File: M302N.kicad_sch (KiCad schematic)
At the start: 35 parts, among them J1 DC12V, J10 ADC_IN, J11 RJ45, J12 DC12V FAN, J13 Conn_01x05_Socket, J14 Conn_01x05_Socket, J15 Conn_01x05_Pin, J16 Conn_01x05_Pin, J17 Conn_01x08_Pin, J18 Conn_01x04_Socket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

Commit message: V2.00はじめ
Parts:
- removed J10, J9: ADC_IN, Connector_JST:JST_XH_B3B-XH-A_1x03_P2.50mm_Vertical, symbol Connector_Generic:Conn_01x03
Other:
- title: M302N -> M302N (under constructions)

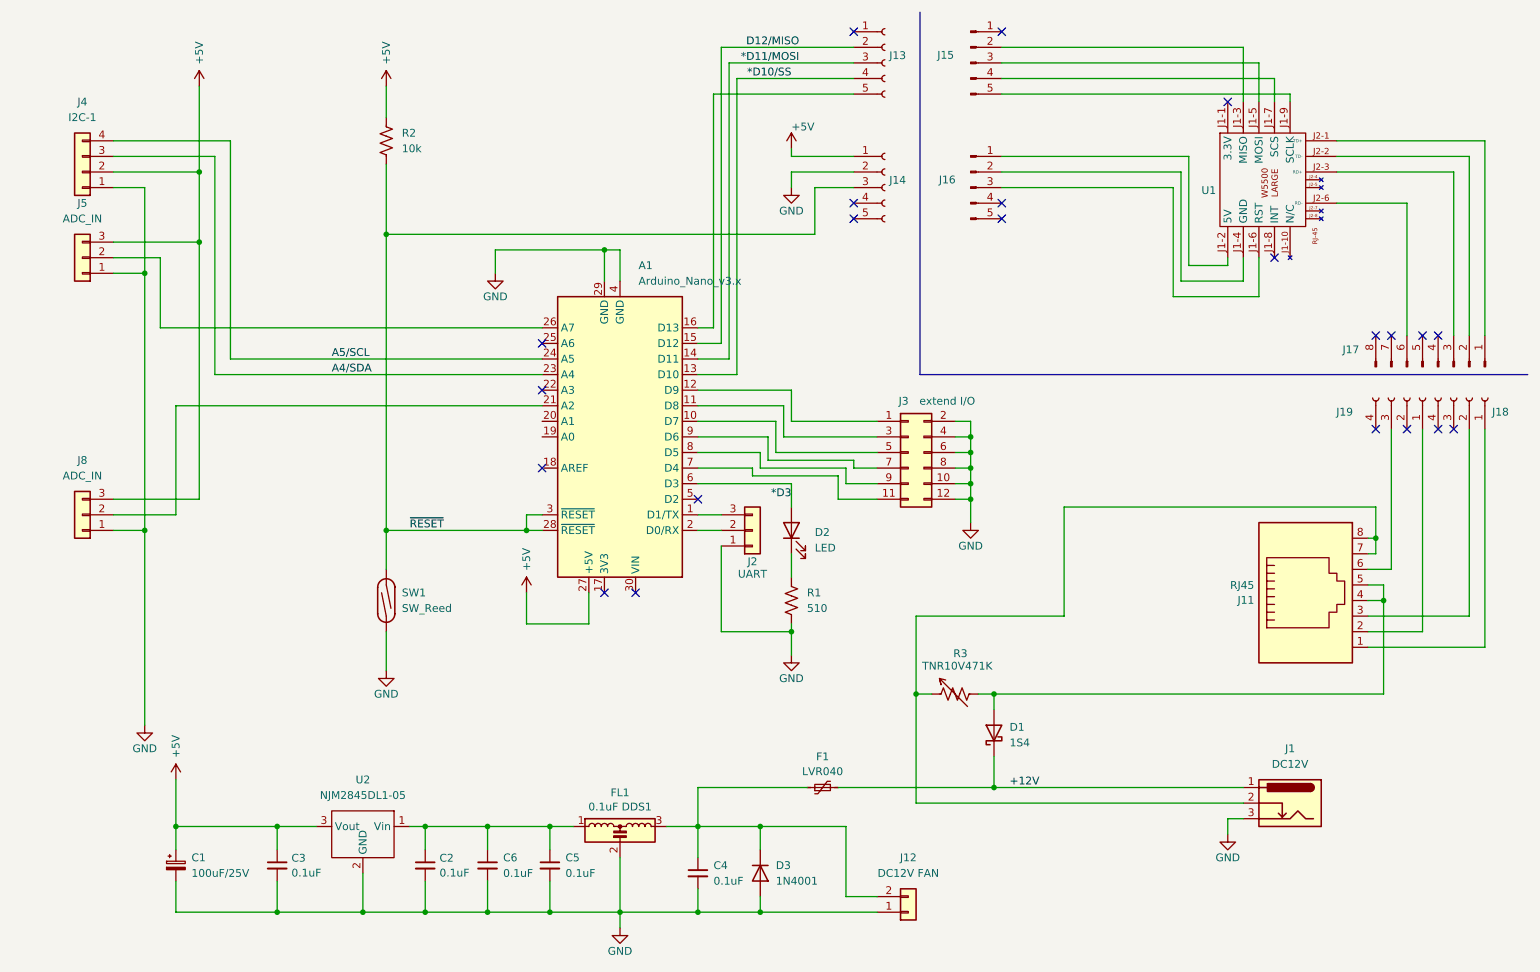
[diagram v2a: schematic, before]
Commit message: 回路図上の変更は完了。PCB部品の選定に入る所。
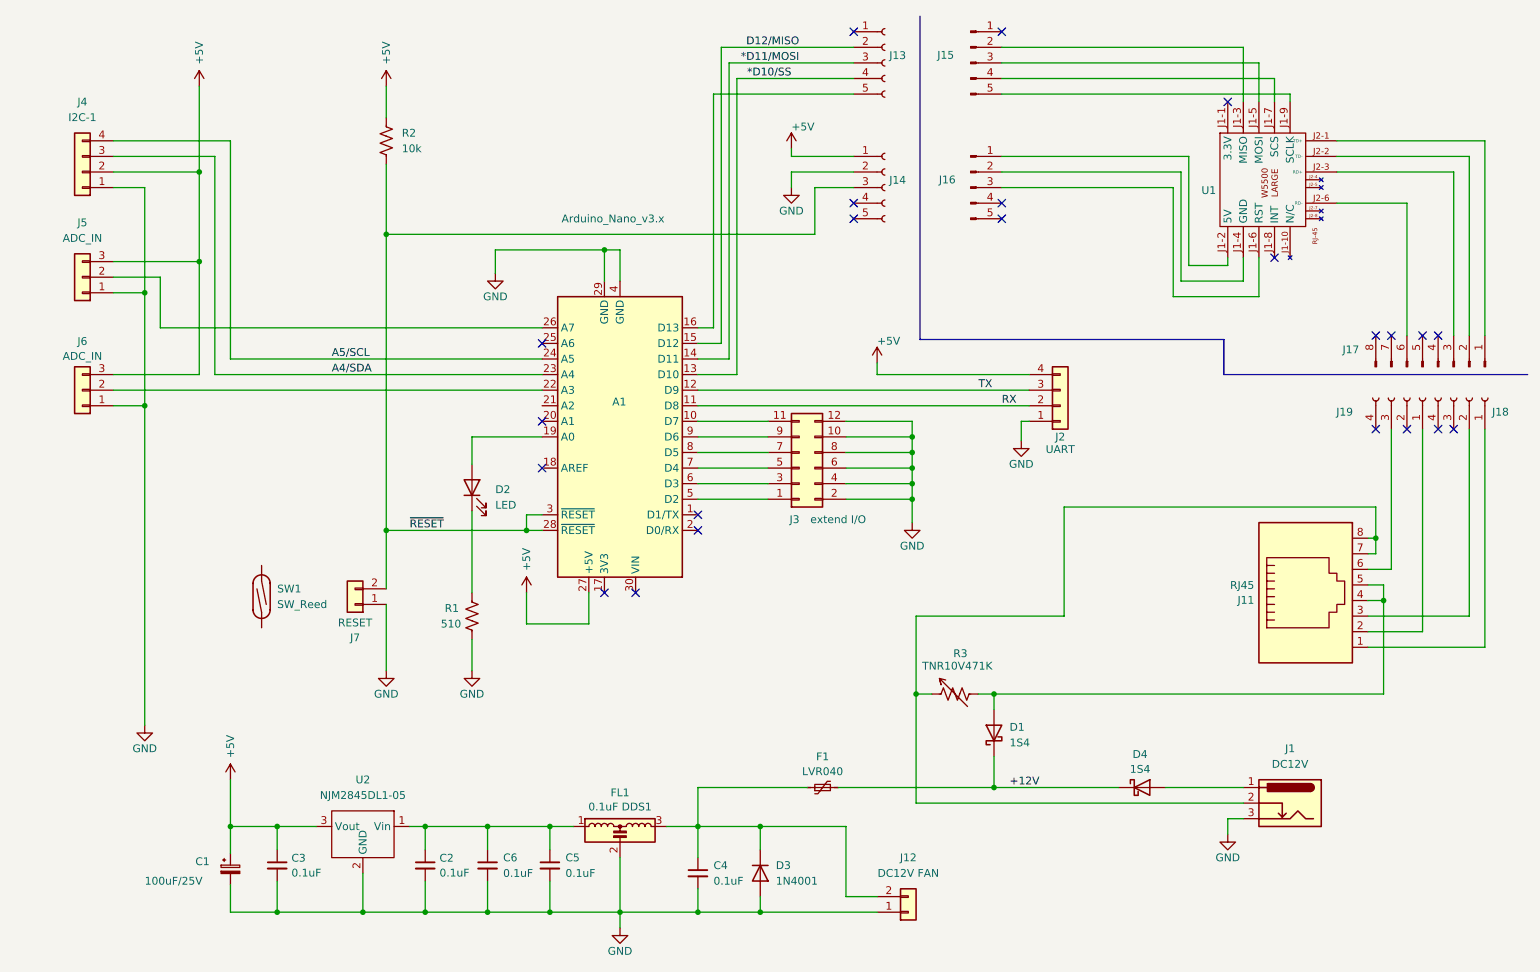
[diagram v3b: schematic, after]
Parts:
- added D4: 1S4, Resistor_THT:R_Axial_DIN0204_L3.6mm_D1.6mm_P5.08mm_Horizontal, symbol Device:D_Schottky
- added J7: RESET, Connector_JST:JST_XH_S2B-XH-A_1x02_P2.50mm_Horizontal, symbol Connector_Generic:Conn_01x02
- J2: footprint Connector_PinHeader_2.54mm:PinHeader_1x03_P2.54mm_Vertical -> Connector_PinHeader_2.54mm:PinHeader_1x04_P2.54mm_Vertical; symbol Connector_Generic:Conn_01x03 -> Connector_Generic:Conn_01x04
- J5: footprint Connector_JST:JST_XH_S3B-XH-A_1x03_P2.50mm_Horizontal -> Connector_JST:JST_XH_B3B-XH-A_1x03_P2.50mm_Vertical
- SW1: now left out of the parts list
- renumbered J8 to J6
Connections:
- net +12V: now also D4.1 (K); no longer J1.1
- net +5V: now also J2.4 (Pin_4)
- net GND: now also J7.1 (Pin_1); no longer SW1.1
- net ~{RESET}: now also J7.2 (Pin_2); no longer SW1.2
- net at A1.2 (D0/RX): no longer J2.2 (Pin_2)
- net at A1.1 (D1/TX): no longer J2.3 (Pin_3)
- net at J3.1 (Pin_1): now also A1.5 (D2); no longer A1.12 (D9)
- net at J3.11 (Pin_11): now also A1.10 (D7); no longer A1.7 (D4)
- net at J3.3 (Pin_3): now also A1.6 (D3); no longer A1.11 (D8)
- net at J3.5 (Pin_5): now also A1.7 (D4); no longer A1.10 (D7)
- net at J3.7 (Pin_7): now also A1.8 (D5); no longer A1.9 (D6)
- net at J3.9 (Pin_9): now also A1.9 (D6); no longer A1.8 (D5)
- net at J6.2 (Pin_2): now also A1.22 (A3); no longer A1.21 (A2)
- net at A1.19 (A0): now also D2.2 (A)
- removed net *D3: A1.6 (D3), D2.2 (A)
- new net: D4.2 (A), J1.1
- new net RX: A1.11 (D8), J2.2 (Pin_2)
- new net TX: A1.12 (D9), J2.3 (Pin_3)
- no-connect marks 22 -> 23
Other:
- moved on the sheet: C1, D2, J3, J5, J6, R1, SW1

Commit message: v2.00 PCB変更とスイッチングレギュレータ採用検討
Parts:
- J2: footprint Connector_PinHeader_2.54mm:PinHeader_1x04_P2.54mm_Vertical -> Connector_JST:JST_XH_S4B-XH-A_1x04_P2.50mm_Horizontal
- J5: footprint Connector_JST:JST_XH_B3B-XH-A_1x03_P2.50mm_Vertical -> Connector_JST:JST_XH_S3B-XH-A_1x03_P2.50mm_Horizontal
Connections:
- no-connect marks 23 -> 24
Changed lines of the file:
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@@
 	)
 	(no_connect
+		(at 123.19 78.74)
+	)
+	(no_connect
 		(at 234.95 29.21)
 	)
@@
 			)
 		)
-		(property "Footprint" "Connector_JST:JST_XH_B3B-XH-A_1x03_P2.50mm_Vertical"
+		(property "Footprint" "Connector_JST:JST_XH_S3B-XH-A_1x03_P2.50mm_Horizontal"
 			(at 48.26 57.785 0)
 			(effects
@@
 			)
 		)
-		(property "Footprint" "Connector_PinHeader_2.54mm:PinHeader_1x04_P2.54mm_Vertical"
+		(property "Footprint" "Connector_JST:JST_XH_S4B-XH-A_1x04_P2.50mm_Horizontal"
 			(at 207.645 78.74 0)
 			(effects

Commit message: DCDC converter
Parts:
- removed C3: 0.1uF, Capacitor_THT:C_Disc_D4.3mm_W1.9mm_P5.00mm, symbol Device:C_Small
- removed U2: NJM2845DL1-05, Package_TO_SOT_SMD:TO-252-3_TabPin2, symbol holly:NJM2845DL1
- added U2: BP5293-50, SIP03_BP5293_17X7P2_ROM, symbol 2025-06-02_10-47-13:BP5293-50
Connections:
- net +5V: now also U2.3 (VOUT)
- net GND: now also U2.2 (GND)
- net at C2.1, C5.1, C6.1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: now also U2.1 (VIN)
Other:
- moved on the sheet: C1

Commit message: 大胆な変更
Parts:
- removed C6: 0.1uF, Capacitor_THT:C_Disc_D4.3mm_W1.9mm_P5.00mm, symbol Device:C_Small
- U2: footprint SIP03_BP5293_17X7P2_ROM -> footprints:SIP03_BP5293_17X7P2_ROM; symbol 2025-06-02_10-47-13:BP5293-50 -> M302N-symlib:BP5293-50
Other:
- moved on the sheet: C2, U2
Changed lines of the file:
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@@
 	)
 	(junction
-		(at 104.14 161.29)
-		(diameter 0)
-		(color 0 0 0 0)
-	)
-	(junction
 		(at 133.35 53.34)
 		(diameter 0)
@@
 	)
 	(junction
-		(at 148.59 161.29)
+		(at 111.76 161.29)
 		(diameter 0)
 		(color 0 0 0 0)
 	)
 	(junction
-		(at 97.79 50.8)
+		(at 111.76 147.32)
 		(diameter 0)
 		(color 0 0 0 0)
 	)
 	(junction
-		(at 183.515 83.82)
+		(at 148.59 161.29)
 		(diameter 0)
 		(color 0 0 0 0)
 	)
 	(junction
-		(at 183.515 93.98)
+		(at 97.79 50.8)
 		(diameter 0)
 		(color 0 0 0 0)
 	)
 	(junction
-		(at 114.3 147.32)
+		(at 183.515 83.82)
 		(diameter 0)
 		(color 0 0 0 0)
 	)
 	(junction
-		(at 260.35 110.49)
+		(at 183.515 93.98)
 		(diameter 0)
 		(color 0 0 0 0)
 	)
 	(junction
-		(at 97.79 99.06)
+		(at 260.35 110.49)
 		(diameter 0)
 		(color 0 0 0 0)
 	)
 	(junction
-		(at 50.8 147.32)
+		(at 97.79 99.06)
 		(diameter 0)
 		(color 0 0 0 0)
 	)
 	(junction
-		(at 114.3 161.29)
+		(at 50.8 147.32)
 		(diameter 0)
 		(color 0 0 0 0)
@@
 	)
 	(junction
-		(at 104.14 147.32)
-		(diameter 0)
-		(color 0 0 0 0)
-	)
-	(junction
 		(at 58.42 161.29)
 		(diameter 0)
@@
 	(wire
 		(pts
-			(xy 50.8 147.32) (xy 60.96 147.32)
+			(xy 50.8 147.32) (xy 68.58 147.32)
 		)
 		(stroke
@@
 	(wire
 		(pts
-			(xy 101.6 147.32) (xy 104.14 147.32)
+			(xy 109.22 147.32) (xy 111.76 147.32)
 		)
 		(stroke
@@
 	(wire
 		(pts
-			(xy 114.3 161.29) (xy 124.46 161.29)
-		)
-		(stroke
-			(width 0)
-			(type default)
-		)
-	)
-	(wire
-		(pts
 			(xy 224.79 140.97) (xy 237.49 140.97)
 		)
@@
 	(wire
 		(pts
-			(xy 58.42 149.86) (xy 60.96 149.86)
-		)
-		(stroke
-			(width 0)
-			(type default)
-		)
-	)
-	(wire
-		(pts
-			(xy 114.3 156.21) (xy 114.3 161.29)
+			(xy 58.42 149.86) (xy 68.58 149.86)
 		)
 		(stroke
@@
 	(wire
 		(pts
-			(xy 104.14 161.29) (xy 114.3 161.29)
-		)
-		(stroke
-			(width 0)
-			(type default)
-		)
-	)
-	(wire
-		(pts
 			(xy 148.59 93.98) (xy 160.02 93.98)
 		)
@@
 	(wire
 		(pts
-			(xy 104.14 147.32) (xy 104.14 151.13)
+			(xy 111.76 147.32) (xy 111.76 151.13)
 		)
 		(stroke
@@
 	(wire
 		(pts
-			(xy 114.3 147.32) (xy 104.14 147.32)
-		)
-		(stroke
-			(width 0)
-			(type default)
-		)
-	)
-	(wire
-		(pts
 			(xy 240.03 22.86) (xy 240.03 29.21)
 		)
@@
 	(wire
 		(pts
-			(xy 58.42 161.29) (xy 104.14 161.29)
+			(xy 58.42 161.29) (xy 111.76 161.29)
 		)
 		(stroke
@@
 	(wire
 		(pts
-			(xy 114.3 147.32) (xy 114.3 151.13)
-		)
-		(stroke
-			(width 0)
-			(type default)
-		)
-	)
-	(wire
-		(pts
 			(xy 257.81 115.57) (xy 266.7 115.57)
 		)
@@
 	(wire
 		(pts
-			(xy 114.3 147.32) (xy 124.46 147.32)
-		)
-		(stroke
-			(width 0)
-			(type default)
-		)
-	)
-	(wire
-		(pts
 			(xy 260.35 110.49) (xy 260.35 107.95)
 		)
@@
 	(wire
 		(pts
-			(xy 104.14 156.21) (xy 104.14 161.29)
+			(xy 111.76 156.21) (xy 111.76 161.29)
 		)
 		(stroke
@@
 	(wire
 		(pts
+			(xy 111.76 161.29) (xy 124.46 161.29)
+		)
+		(stroke
+			(width 0)
+			(type default)
+		)
+	)
+	(wire
+		(pts
 			(xy 228.6 38.1) (xy 228.6 55.88)
 		)
@@
 	(wire
 		(pts
+			(xy 111.76 147.32) (xy 124.46 147.32)
+		)
+		(stroke
+			(width 0)
+			(type default)
+		)
+	)
+	(wire
+		(pts
 			(xy 264.16 67.31) (xy 264.16 45.72)
 		)
@@
 	)
 	(symbol
-		(lib_id "2025-06-02_10-47-13:BP5293-50")
-		(at 101.6 147.32 0)
+		(lib_id "M302N-symlib:BP5293-50")
+		(at 109.22 147.32 0)
 		(mirror y)
 		(unit 1)
@@
 		(fields_autoplaced yes)
 		(property "Reference" "U2"
-			(at 81.28 137.5461 0)
+			(at 88.9 137.5461 0)
 			(effects
 				(font
@@
 		)
 		(property "Value" "BP5293-50"
-			(at 81.28 140.379 0)
+			(at 88.9 140.379 0)
 			(effects
 				(font
@@
 			)
 		)
-		(property "Footprint" "SIP03_BP5293_17X7P2_ROM"
-			(at 101.6 147.32 0)
+		(property "Footprint" "footprints:SIP03_BP5293_17X7P2_ROM"
+			(at 109.22 147.32 0)
 			(effects
 				(font
@@
 		)
 		(property "Datasheet" "BP5293-50"
-			(at 101.6 147.32 0)
+			(at 109.22 147.32 0)
 			(effects
 				(font
@@
 		)
 		(property "Description" ""
-			(at 101.6 147.32 0)
+			(at 109.22 147.32 0)
 			(effects
 				(font
@@
 	(symbol
 		(lib_id "Device:C_Small")
-		(at 104.14 153.67 0)
+		(at 111.76 153.67 0)
 		(unit 1)
 		(exclude_from_sim no)
@@
 		(dnp no)
 		(property "Reference" "C2"
-			(at 106.4641 152.4641 0)
+			(at 114.0841 152.4641 0)
 			(effects
 				(font
@@
 		)
 		(property "Value" "0.1uF"
-			(at 106.4641 154.8884 0)
+			(at 114.0841 154.8884 0)
 			(effects
 				(font
@@
 		)
 		(property "Footprint" "Capacitor_THT:C_Disc_D4.3mm_W1.9mm_P5.00mm"
-			(at 104.14 153.67 0)
+			(at 111.76 153.67 0)
 			(effects
 				(font
@@
 		)
 		(property "Datasheet" "~"
-			(at 104.14 153.67 0)
+			(at 111.76 153.67 0)
 			(effects
 				(font
@@
 		)
 		(property "Description" "Unpolarized capacitor, small symbol"
-			(at 104.14 153.67 0)
+			(at 111.76 153.67 0)
 			(effects
 				(font
@@
 					(unit 1)
 				)
-			)
-		)
-	)
-	(symbol
-		(lib_id "Device:C_Small")
-		(at 114.3 153.67 0)
-		(unit 1)
-		(exclude_from_sim no)
-		(in_bom yes)
-		(on_board yes)
-		(dnp no)
-		(fields_autoplaced yes)
-		(property "Reference" "C6"
-			(at 116.84 152.4062 0)
-			(effects
-				(font
-					(size 1.27 1.27)
-				)
-				(justify left)
-			)
-		)
-		(property "Value" "0.1uF"
-			(at 116.84 154.9462 0)
-			(effects
-				(font
-					(size 1.27 1.27)
-				)
-				(justify left)
-			)
-		)
-		(property "Footprint" "Capacitor_THT:C_Disc_D4.3mm_W1.9mm_P5.00mm"
-			(at 114.3 153.67 0)
-			(effects
-				(font
-					(size 1.27 1.27)
-				)
-				(hide yes)
-			)
-		)
-		(property "Datasheet" "~"
-			(at 114.3 153.67 0)
-			(effects
-				(font
-					(size 1.27 1.27)
-				)
-				(hide yes)
-			)
-		)
-		(property "Description" "Unpolarized capacitor, small symbol"
-			(at 114.3 153.67 0)
-			(effects
-				(font
-					(size 1.27 1.27)
-				)
-				(hide yes)
-			)
-		)
-		(pin "2"
-		)
-		(pin "1"
-		)
-		(instances
-			(project "M302N"
-				(path "/0d35483a-0b12-46cc-b9f2-896fd6831779"
-					(reference "C6")
-					(unit 1)
-				)
